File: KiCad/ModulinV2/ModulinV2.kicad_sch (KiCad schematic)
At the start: 0 parts

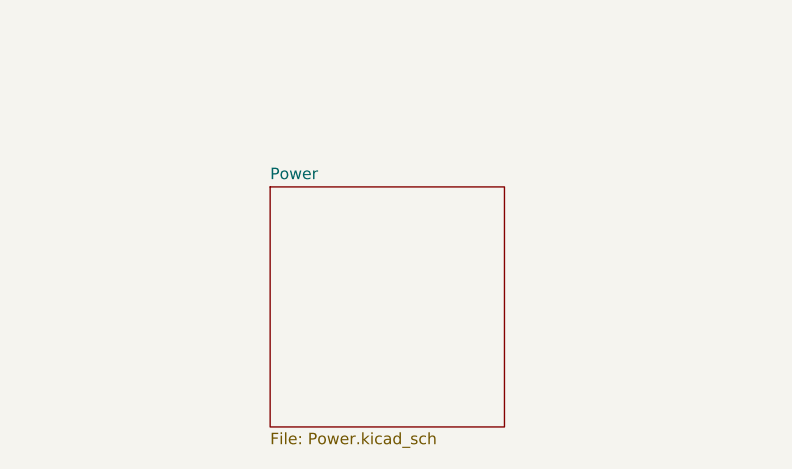
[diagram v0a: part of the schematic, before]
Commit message: Fleshed out the waveform select schematic a bit + general cleanup
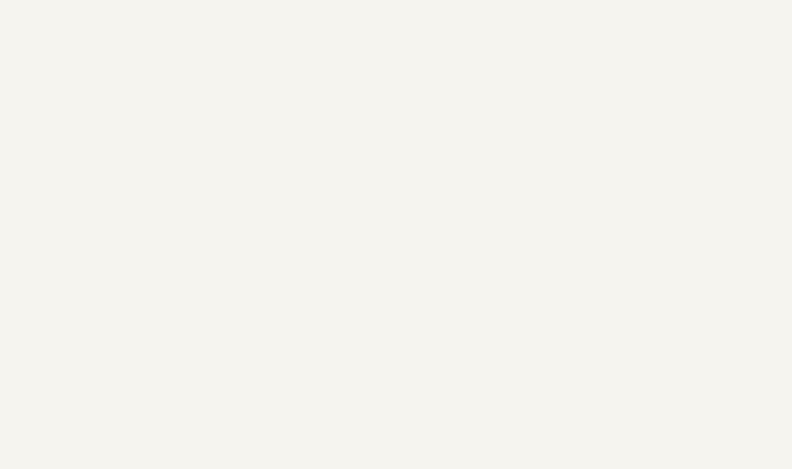
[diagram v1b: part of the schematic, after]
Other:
- removed sheet Power
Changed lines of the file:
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@@
-	)
-	(sheet
-		(at 49.53 151.765)
-		(size 26.035 26.67)
-		(exclude_from_sim no)
-		(in_bom yes)
-		(on_board yes)
-		(dnp no)
-		(fields_autoplaced yes)
-		(stroke
-			(width 0.1524)
-			(type solid)
-		)
-		(fill
-			(color 0 0 0 0.0000)
-		)
-		(property "Sheetname" "Power"
-			(at 49.53 151.0534 0)
-			(effects
-				(font
-					(size 1.27 1.27)
-				)
-				(justify left bottom)
-			)
-		)
-		(property "Sheetfile" "Power.kicad_sch"
-			(at 49.53 179.0196 0)
-			(effects
-				(font
-					(size 1.27 1.27)
-				)
-				(justify left top)
-			)
-		)
-		(instances
-			(project "ModulinV2"
-				(path "/c6b34a57-3941-4b56-8b80-1848c7f41082"
-					(page "8")
-				)
-			)
-		)
 	)
 	(sheet

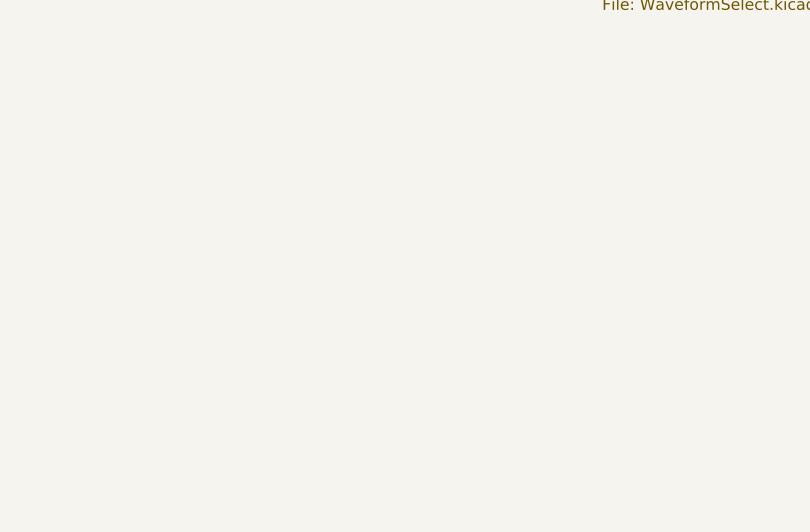
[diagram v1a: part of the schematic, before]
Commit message: Added initial power supply schematic and modified MCU components
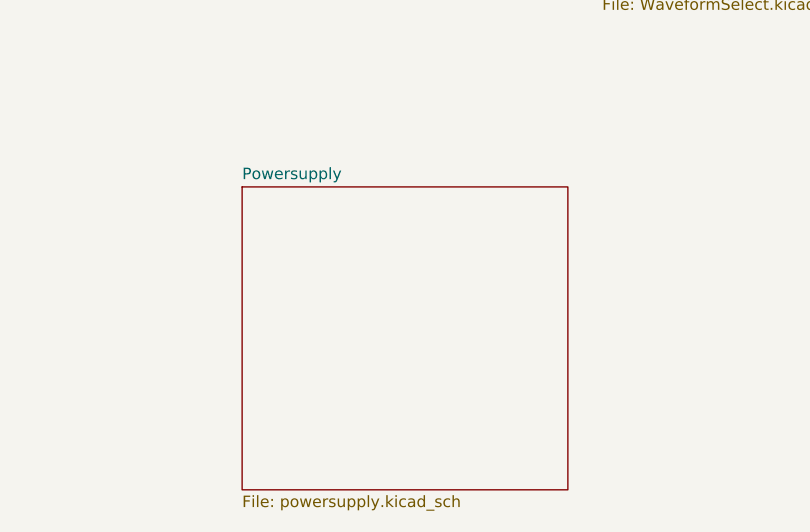
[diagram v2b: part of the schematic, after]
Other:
- added sheet Powersupply (powersupply.kicad_sch)
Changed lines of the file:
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@@
+		)
+	)
+	(sheet
+		(at 61.595 146.685)
+		(size 36.195 33.655)
+		(exclude_from_sim no)
+		(in_bom yes)
+		(on_board yes)
+		(dnp no)
+		(fields_autoplaced yes)
+		(stroke
+			(width 0.1524)
+			(type solid)
+		)
+		(fill
+			(color 0 0 0 0.0000)
+		)
+		(property "Sheetname" "Powersupply"
+			(at 61.595 145.9734 0)
+			(effects
+				(font
+					(size 1.27 1.27)
+				)
+				(justify left bottom)
+			)
+		)
+		(property "Sheetfile" "powersupply.kicad_sch"
+			(at 61.595 180.9246 0)
+			(effects
+				(font
+					(size 1.27 1.27)
+				)
+				(justify left top)
+			)
+		)
+		(instances
+			(project "ModulinV2"
+				(path "/c6b34a57-3941-4b56-8b80-1848c7f41082"
+					(page "8")
+				)
+			)
 		)
 	)

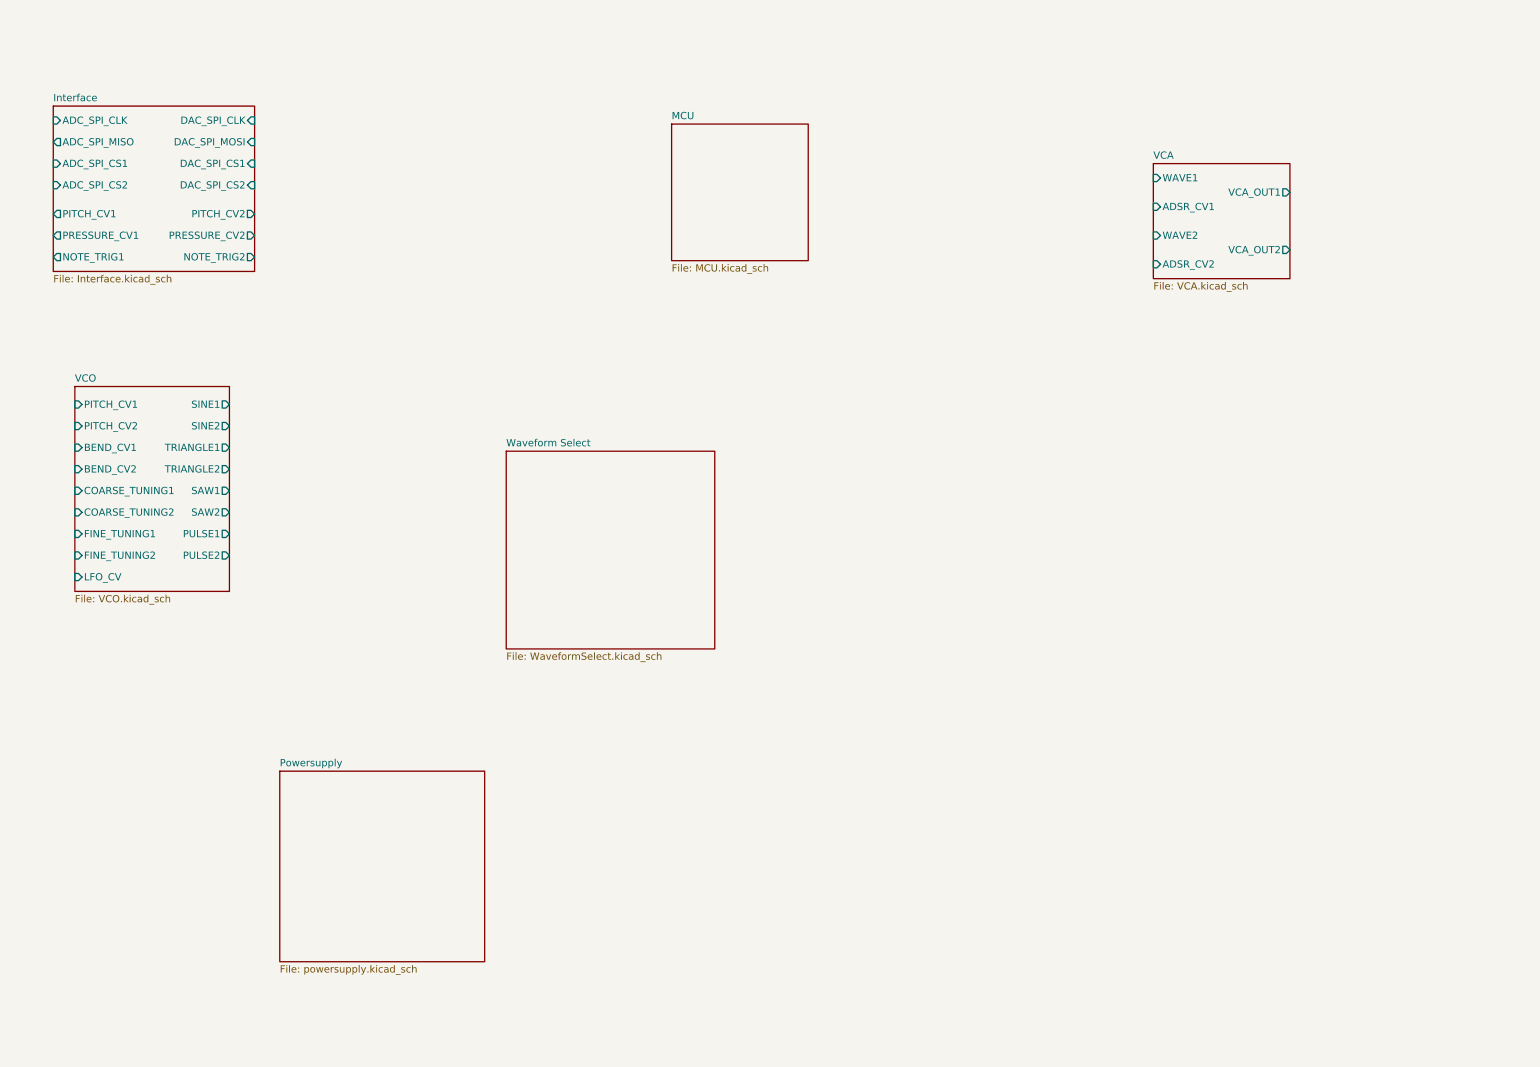
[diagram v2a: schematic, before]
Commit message: Designed ADSR and better tuning schematics with digital/manual capability
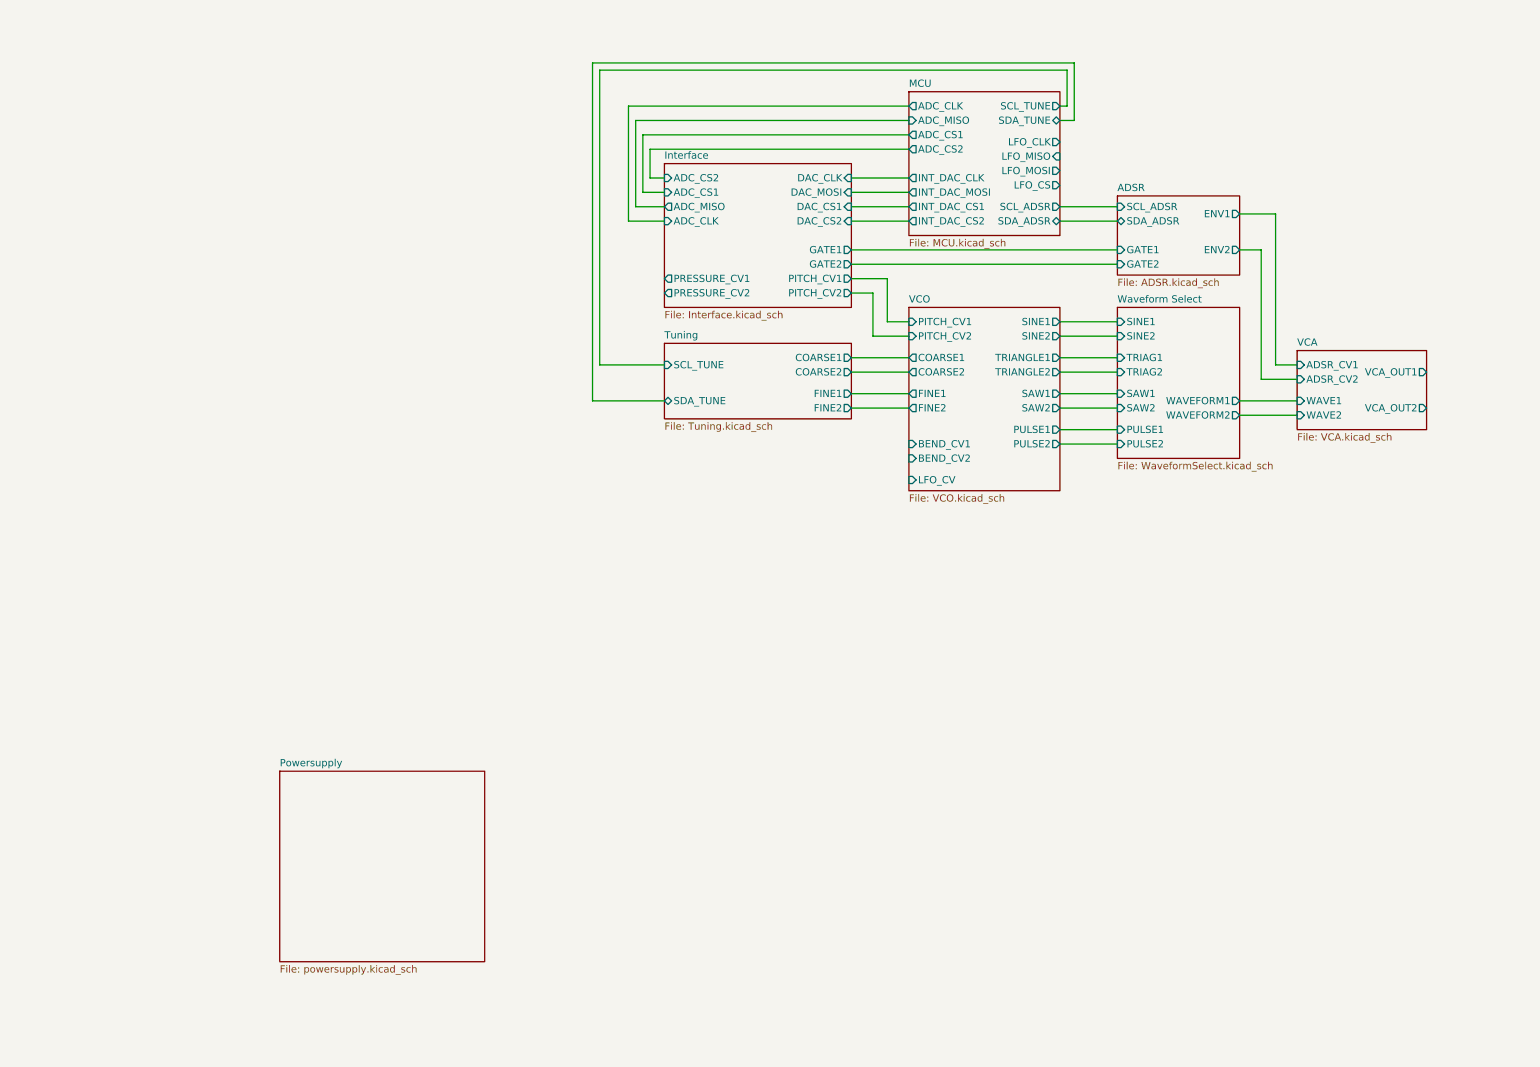
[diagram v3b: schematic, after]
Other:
- added sheet ADSR (ADSR.kicad_sch)
- added sheet Tuning (Tuning.kicad_sch)
- sheet Interface ports: added ADC_CLK, ADC_CS1, ADC_CS2, ADC_MISO, DAC_CLK, DAC_CS1, DAC_CS2, DAC_MOSI, GATE1, GATE2; removed ADC_SPI_CLK, ADC_SPI_CS1, ADC_SPI_CS2, ADC_SPI_MISO, DAC_SPI_CLK, DAC_SPI_CS1, DAC_SPI_CS2, DAC_SPI_MOSI, NOTE_TRIG1, NOTE_TRIG2
- sheet MCU ports: added ADC_CLK, ADC_CS1, ADC_CS2, ADC_MISO, INT_DAC_CLK, INT_DAC_CS1, INT_DAC_CS2, INT_DAC_MOSI, LFO_CLK, LFO_CS, LFO_MISO, LFO_MOSI, SCL_ADSR, SCL_TUNE, SDA_ADSR, SDA_TUNE; removed none
- sheet VCO ports: added COARSE1, COARSE2, FINE1, FINE2; removed COARSE_TUNING1, COARSE_TUNING2, FINE_TUNING1, FINE_TUNING2
- sheet Waveform Select ports: added PULSE1, PULSE2, SAW1, SAW2, SINE1, SINE2, TRIAG1, TRIAG2, WAVEFORM1, WAVEFORM2; removed none

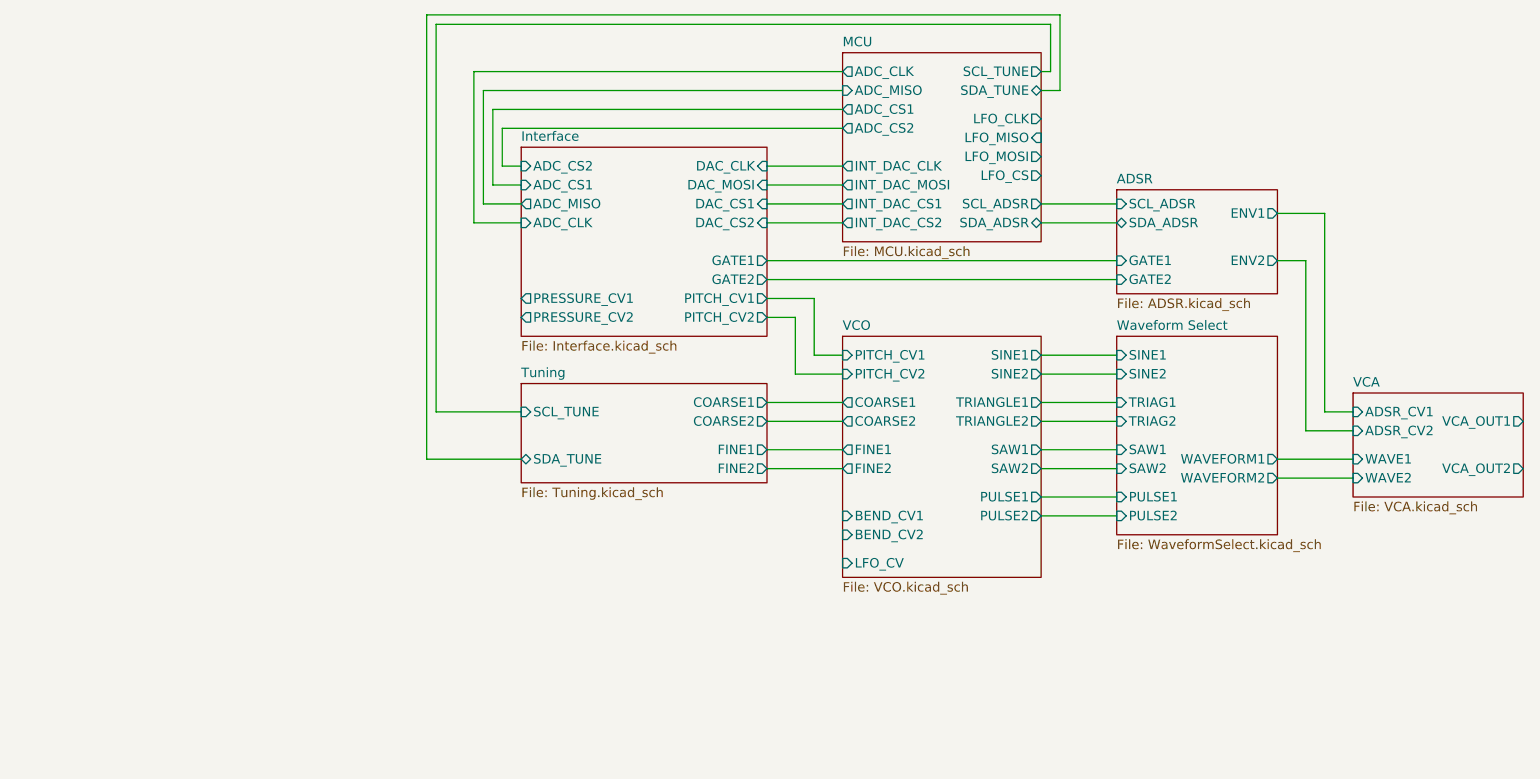
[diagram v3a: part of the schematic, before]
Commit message: Added 4k7 pullups to I2C lines
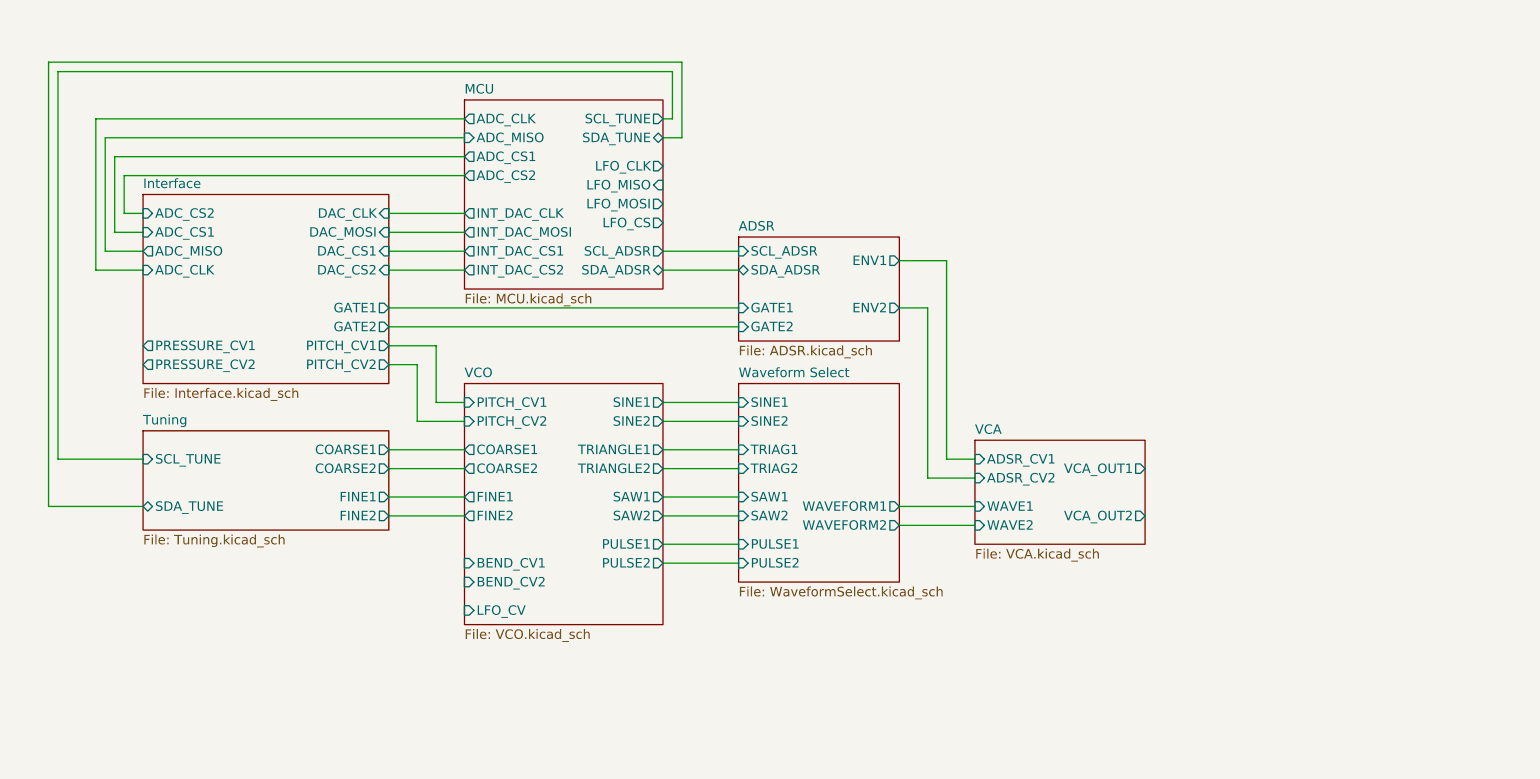
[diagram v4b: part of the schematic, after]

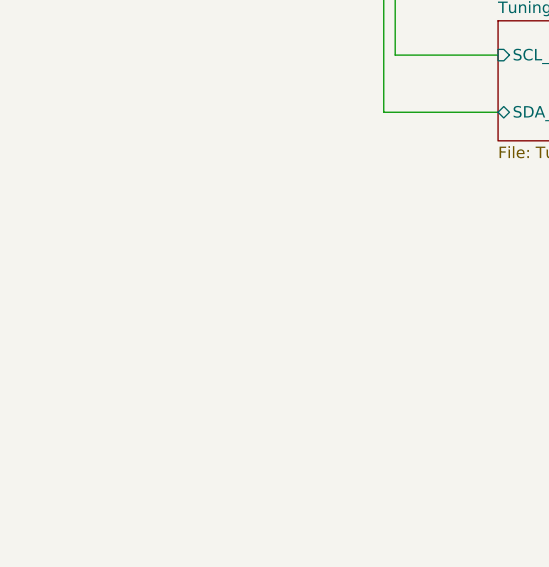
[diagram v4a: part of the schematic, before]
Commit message: Found and added linear slide pot meant for pitch bending
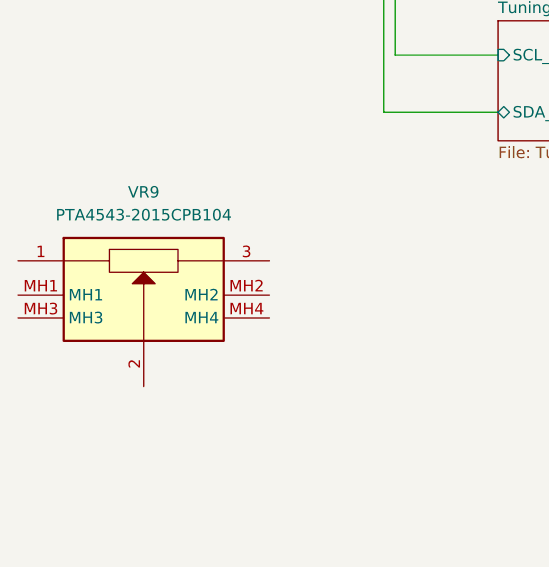
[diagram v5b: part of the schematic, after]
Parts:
- added VR9: PTA4543-2015CPB104, PTA45432015CPB503, symbol PTA4543-2015CPB104:PTA4543-2015CPB104
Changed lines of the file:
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@@
+		)
+	)
+	(symbol
+		(lib_id "PTA4543-2015CPB104:PTA4543-2015CPB104")
+		(at 25.4 104.14 0)
+		(unit 1)
+		(exclude_from_sim no)
+		(in_bom yes)
+		(on_board yes)
+		(dnp no)
+		(fields_autoplaced yes)
+		(property "Reference" "VR9"
+			(at 39.37 96.52 0)
+			(effects
+				(font
+					(size 1.27 1.27)
+				)
+			)
+		)
+		(property "Value" "PTA4543-2015CPB104"
+			(at 39.37 99.06 0)
+			(effects
+				(font
+					(size 1.27 1.27)
+				)
+			)
+		)
+		(property "Footprint" "PTA45432015CPB503"
+			(at 49.53 191.44 0)
+			(effects
+				(font
+					(size 1.27 1.27)
+				)
+				(justify left top)
+				(hide yes)
+			)
+		)
+		(property "Datasheet" "https://componentsearchengine.com/Datasheets/1/PTA4543-2015CPB503.pdf"
+			(at 49.53 291.44 0)
+			(effects
+				(font
+					(size 1.27 1.27)
+				)
+				(justify left top)
+				(hide yes)
+			)
+		)
+		(property "Description" "Low profile slide potentionmeter"
+			(at 33.274 97.79 0)
+			(effects
+				(font
+					(size 1.27 1.27)
+				)
+				(hide yes)
+			)
+		)
+		(property "Height" "21.5"
+			(at 49.53 491.44 0)
+			(effects
+				(font
+					(size 1.27 1.27)
+				)
+				(justify left top)
+				(hide yes)
+			)
+		)
+		(property "Manufacturer_Name" "Bourns"
+			(at 49.53 591.44 0)
+			(effects
+				(font
+					(size 1.27 1.27)
+				)
+				(justify left top)
+				(hide yes)
+			)
+		)
+		(property "Manufacturer_Part_Number" "PTA4543-2015CPB104"
+			(at 49.53 691.44 0)
+			(effects
+				(font
+					(size 1.27 1.27)
+				)
+				(justify left top)
+				(hide yes)
+			)
+		)
+		(property "Mouser Part Number" "652-PTA45432015CPB10"
+			(at 49.53 791.44 0)
+			(effects
+				(font
+					(size 1.27 1.27)
+				)
+				(justify left top)
+				(hide yes)
+			)
+		)
+		(property "Mouser Price/Stock" "https://www.mouser.co.uk/ProductDetail/Bourns/PTA4543-2015CPB104?qs=Zq5ylnUbLm5bgYHDzxuH5g%3D%3D"
+			(at 49.53 891.44 0)
+			(effects
+				(font
+					(size 1.27 1.27)
+				)
+				(justify left top)
+				(hide yes)
+			)
+		)
+		(property "Arrow Part Number" ""
+			(at 49.53 991.44 0)
+			(effects
+				(font
+					(size 1.27 1.27)
+				)
+				(justify left top)
+				(hide yes)
+			)
+		)
+		(property "Arrow Price/Stock" ""
+			(at 49.53 1091.44 0)
+			(effects
+				(font
+					(size 1.27 1.27)
+				)
+				(justify left top)
+				(hide yes)
+			)
+		)
+		(pin "MH1"
+		)
+		(pin "3"
+		)
+		(pin "MH3"
+		)
+		(pin "2"
+		)
+		(pin "MH2"
+		)
+		(pin "MH4"
+		)
+		(pin "1"
+		)
+		(instances
+			(project ""
+				(path "/c6b34a57-3941-4b56-8b80-1848c7f41082"
+					(reference "VR9")
+					(unit 1)
+				)
+			)
 		)
 	)
